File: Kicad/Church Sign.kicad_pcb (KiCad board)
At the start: 2 copper layers, 50 x 35 mm, 8 parts, among them J1 ESP Header, J2 To LEDs, J3 5V In, U1 AZ1117-3.3

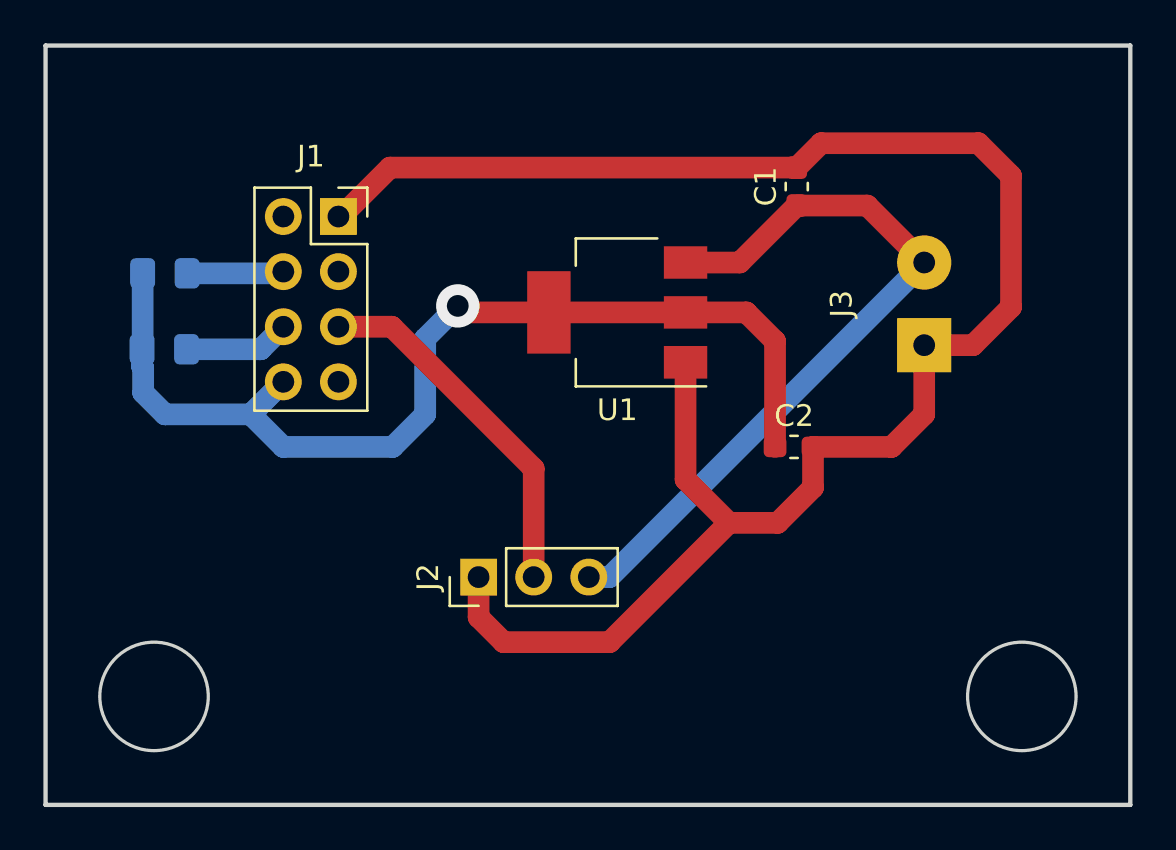
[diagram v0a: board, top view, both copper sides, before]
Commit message: Changes
Moved ESP header traces to back layer.
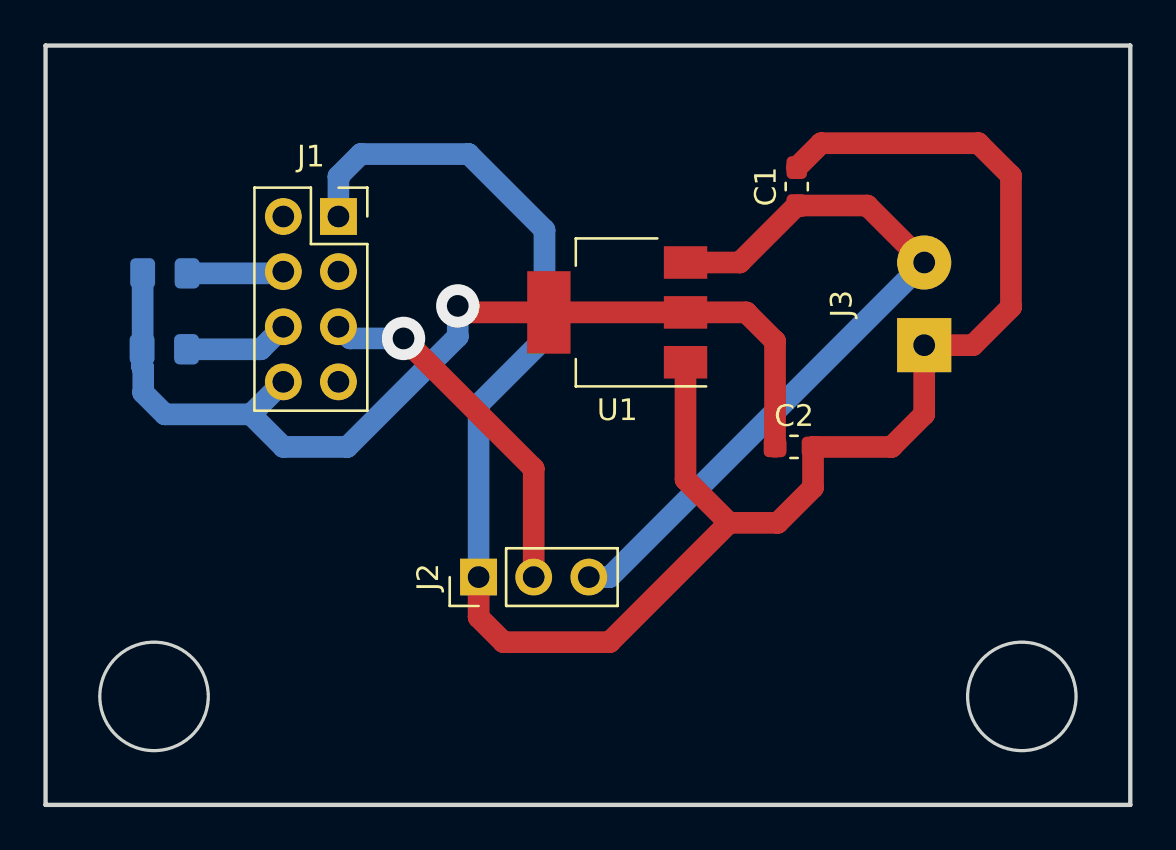
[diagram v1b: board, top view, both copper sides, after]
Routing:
- net GND: track 83.5 -> 92.0 mm
- net +3V3: track 48.1 -> 46.9 mm
- net /LED_DATA: vias 0 -> 1
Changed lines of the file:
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@@
     (thickness 1.6)
     (drawings 6)
-    (tracks 54)
+    (tracks 59)
     (zones 0)
     (modules 8)
@@
     (pad_to_mask_clearance 0.2)
     (aux_axis_origin 0 0)
-    (visible_elements FFFFFF7F)
+    (visible_elements 7FFFFFFF)
     (pcbplotparams
       (layerselection 0x010fc_ffffffff)
@@
   (segment (start 150.5 68.81) (end 152.74968 68.81) (width 1) (layer F.Cu) (net 2))
   (segment (start 152.74968 68.81) (end 154.5 67.05968) (width 1) (layer F.Cu) (net 2))
-  (segment (start 123.62 62.88) (end 123.5 62.88) (width 1) (layer F.Cu) (net 2))
-  (segment (start 144.625 60.625) (end 125.875 60.625) (width 1) (layer F.Cu) (net 2))
-  (segment (start 125.875 60.625) (end 123.62 62.88) (width 1) (layer F.Cu) (net 2))
   (segment (start 129.96 81.35) (end 131.11 82.5) (width 1) (layer F.Cu) (net 2))
   (segment (start 129.96 79.5) (end 129.96 81.35) (width 1) (layer F.Cu) (net 2))
   (segment (start 136 82.5) (end 141.5 77) (width 1) (layer F.Cu) (net 2))
   (segment (start 131.11 82.5) (end 136 82.5) (width 1) (layer F.Cu) (net 2))
+  (segment (start 129.96 71.54) (end 129.96 79.5) (width 1) (layer B.Cu) (net 2))
+  (segment (start 123.5 61.03) (end 124.53 60) (width 1) (layer B.Cu) (net 2))
+  (segment (start 123.5 62.88) (end 123.5 61.03) (width 1) (layer B.Cu) (net 2))
+  (segment (start 129.5 60) (end 133 63.5) (width 1) (layer B.Cu) (net 2))
+  (segment (start 124.53 60) (end 129.5 60) (width 1) (layer B.Cu) (net 2))
+  (segment (start 133 63.5) (end 133 68.5) (width 1) (layer B.Cu) (net 2))
+  (segment (start 133 68.5) (end 129.96 71.54) (width 1) (layer B.Cu) (net 2))
   (segment (start 114.475 68.975) (end 114.45 69) (width 1) (layer B.Cu) (net 3))
   (segment (start 114.475 65.5) (end 114.475 68.975) (width 1) (layer B.Cu) (net 3))
@@
   (segment (start 133.2 67.3) (end 129.3 67.3) (width 1) (layer F.Cu) (net 3))
   (segment (start 129.3 67.3) (end 129 67) (width 1) (layer F.Cu) (net 3))
+  (segment (start 123.914213 73.5) (end 120.96 73.5) (width 1) (layer B.Cu) (net 3))
   (segment (start 120.96 73.5) (end 119.46 72) (width 1) (layer B.Cu) (net 3))
-  (segment (start 126 73.5) (end 120.96 73.5) (width 1) (layer B.Cu) (net 3))
-  (segment (start 127.5 72) (end 126 73.5) (width 1) (layer B.Cu) (net 3))
-  (segment (start 129 67) (end 127.5 68.5) (width 1) (layer B.Cu) (net 3))
-  (segment (start 127.5 68.5) (end 127.5 72) (width 1) (layer B.Cu) (net 3))
+  (segment (start 129 68.414213) (end 123.914213 73.5) (width 1) (layer B.Cu) (net 3))
+  (segment (start 129 67) (end 129 68.414213) (width 1) (layer B.Cu) (net 3))
   (segment (start 120.88 65.5) (end 120.96 65.42) (width 1) (layer B.Cu) (net 4))
   (segment (start 116.525 65.5) (end 120.88 65.5) (width 1) (layer B.Cu) (net 4))
-  (segment (start 123.5 67.96) (end 125.96 67.96) (width 1) (layer F.Cu) (net 5))
-  (segment (start 132.5 74.5) (end 132.5 79.5) (width 1) (layer F.Cu) (net 5))
-  (segment (start 125.96 67.96) (end 132.5 74.5) (width 1) (layer F.Cu) (net 5))
+  (via (at 126.5 68.5) (size 2) (drill 1) (layers F.Cu B.Cu) (net 5))
+  (segment (start 132.5 79.5) (end 132.5 74.5) (width 1) (layer F.Cu) (net 5))
+  (segment (start 132.5 74.5) (end 126.5 68.5) (width 1) (layer F.Cu) (net 5))
+  (segment (start 124.04 68.5) (end 123.5 67.96) (width 1) (layer B.Cu) (net 5))
+  (segment (start 126.5 68.5) (end 124.04 68.5) (width 1) (layer B.Cu) (net 5))
   (segment (start 119.92 69) (end 120.96 67.96) (width 1) (layer B.Cu) (net 6))
   (segment (start 116.5 69) (end 119.92 69) (width 1) (layer B.Cu) (net 6))

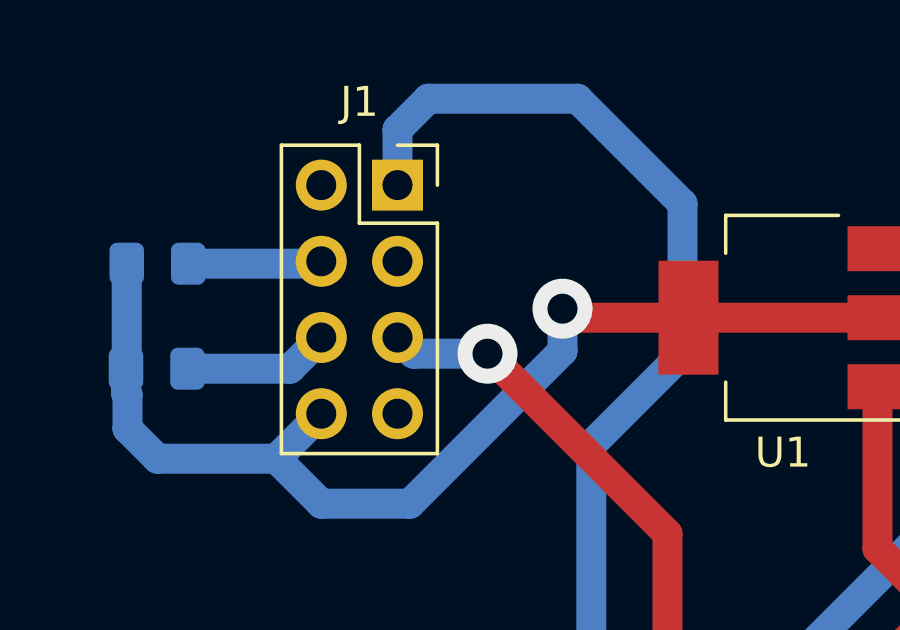
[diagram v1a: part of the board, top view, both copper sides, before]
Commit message: Moved LED Pin
Moved the LED data pin from IO0 to IO2.
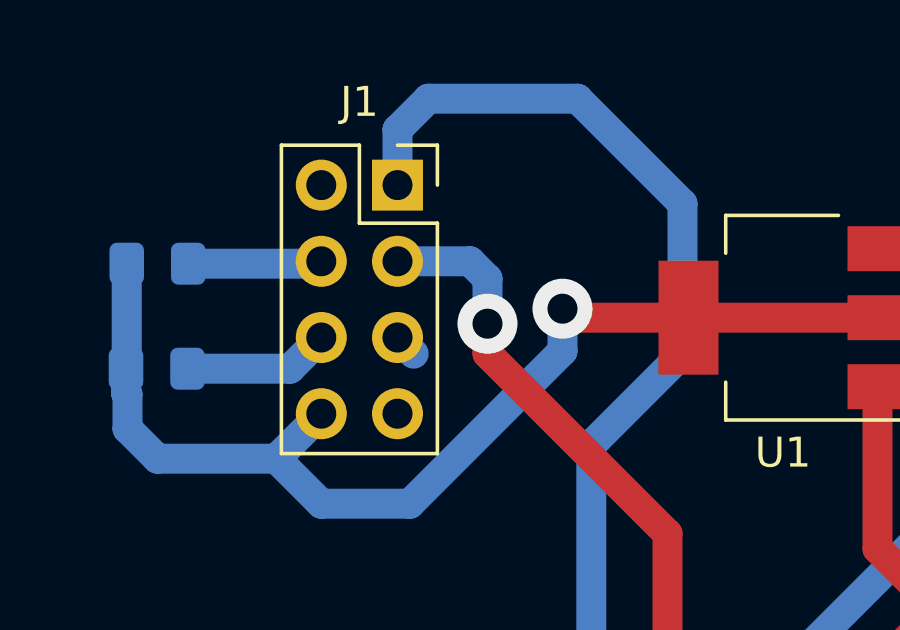
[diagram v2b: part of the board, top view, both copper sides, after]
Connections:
- J1 pad 3: (no net) -> /LED_DATA
- J1 pad 5: /LED_DATA -> (no net)
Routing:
- net /LED_DATA: track 16.7 -> 19.2 mm
- net (no net): track 0.00 -> 0.76 mm
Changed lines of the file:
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@@
     (thickness 1.6)
     (drawings 6)
-    (tracks 59)
+    (tracks 62)
     (zones 0)
     (modules 8)
@@
       (net 2 GND))
     (pad 2 thru_hole oval (at -2.54 0) (size 1.7 1.7) (drill 1) (layers *.Cu *.Mask))
-    (pad 3 thru_hole oval (at 0 2.54) (size 1.7 1.7) (drill 1) (layers *.Cu *.Mask))
+    (pad 3 thru_hole oval (at 0 2.54) (size 1.7 1.7) (drill 1) (layers *.Cu *.Mask)
+      (net 5 /LED_DATA))
     (pad 4 thru_hole oval (at -2.54 2.54) (size 1.7 1.7) (drill 1) (layers *.Cu *.Mask)
       (net 4 "Net-(J1-Pad4)"))
-    (pad 5 thru_hole oval (at 0 5.08) (size 1.7 1.7) (drill 1) (layers *.Cu *.Mask)
-      (net 5 /LED_DATA))
+    (pad 5 thru_hole oval (at 0 5.08) (size 1.7 1.7) (drill 1) (layers *.Cu *.Mask))
     (pad 6 thru_hole oval (at -2.54 5.08) (size 1.7 1.7) (drill 1) (layers *.Cu *.Mask)
       (net 6 "Net-(J1-Pad6)"))
@@
   (segment (start 120.88 65.5) (end 120.96 65.42) (width 1) (layer B.Cu) (net 4))
   (segment (start 116.525 65.5) (end 120.88 65.5) (width 1) (layer B.Cu) (net 4))
-  (via (at 126.5 68.5) (size 2) (drill 1) (layers F.Cu B.Cu) (net 5))
   (segment (start 132.5 79.5) (end 132.5 74.5) (width 1) (layer F.Cu) (net 5))
   (segment (start 132.5 74.5) (end 126.5 68.5) (width 1) (layer F.Cu) (net 5))
-  (segment (start 124.04 68.5) (end 123.5 67.96) (width 1) (layer B.Cu) (net 5))
-  (segment (start 126.5 68.5) (end 124.04 68.5) (width 1) (layer B.Cu) (net 5))
+  (segment (start 124.04 68.5) (end 123.5 67.96) (width 1) (layer B.Cu) (net 0))
+  (via (at 126.5 67.5) (size 2) (drill 1) (layers F.Cu B.Cu) (net 5))
+  (segment (start 126.5 68.5) (end 126.5 67.5) (width 1) (layer F.Cu) (net 5))
+  (segment (start 125.92 65.42) (end 123.5 65.42) (width 1) (layer B.Cu) (net 5))
+  (segment (start 126.5 67.5) (end 126.5 66) (width 1) (layer B.Cu) (net 5))
+  (segment (start 126.5 66) (end 125.92 65.42) (width 1) (layer B.Cu) (net 5))
   (segment (start 119.92 69) (end 120.96 67.96) (width 1) (layer B.Cu) (net 6))
   (segment (start 116.5 69) (end 119.92 69) (width 1) (layer B.Cu) (net 6))
